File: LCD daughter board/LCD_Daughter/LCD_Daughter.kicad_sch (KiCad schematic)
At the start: 12 parts, among them J1 JST EH 9pos

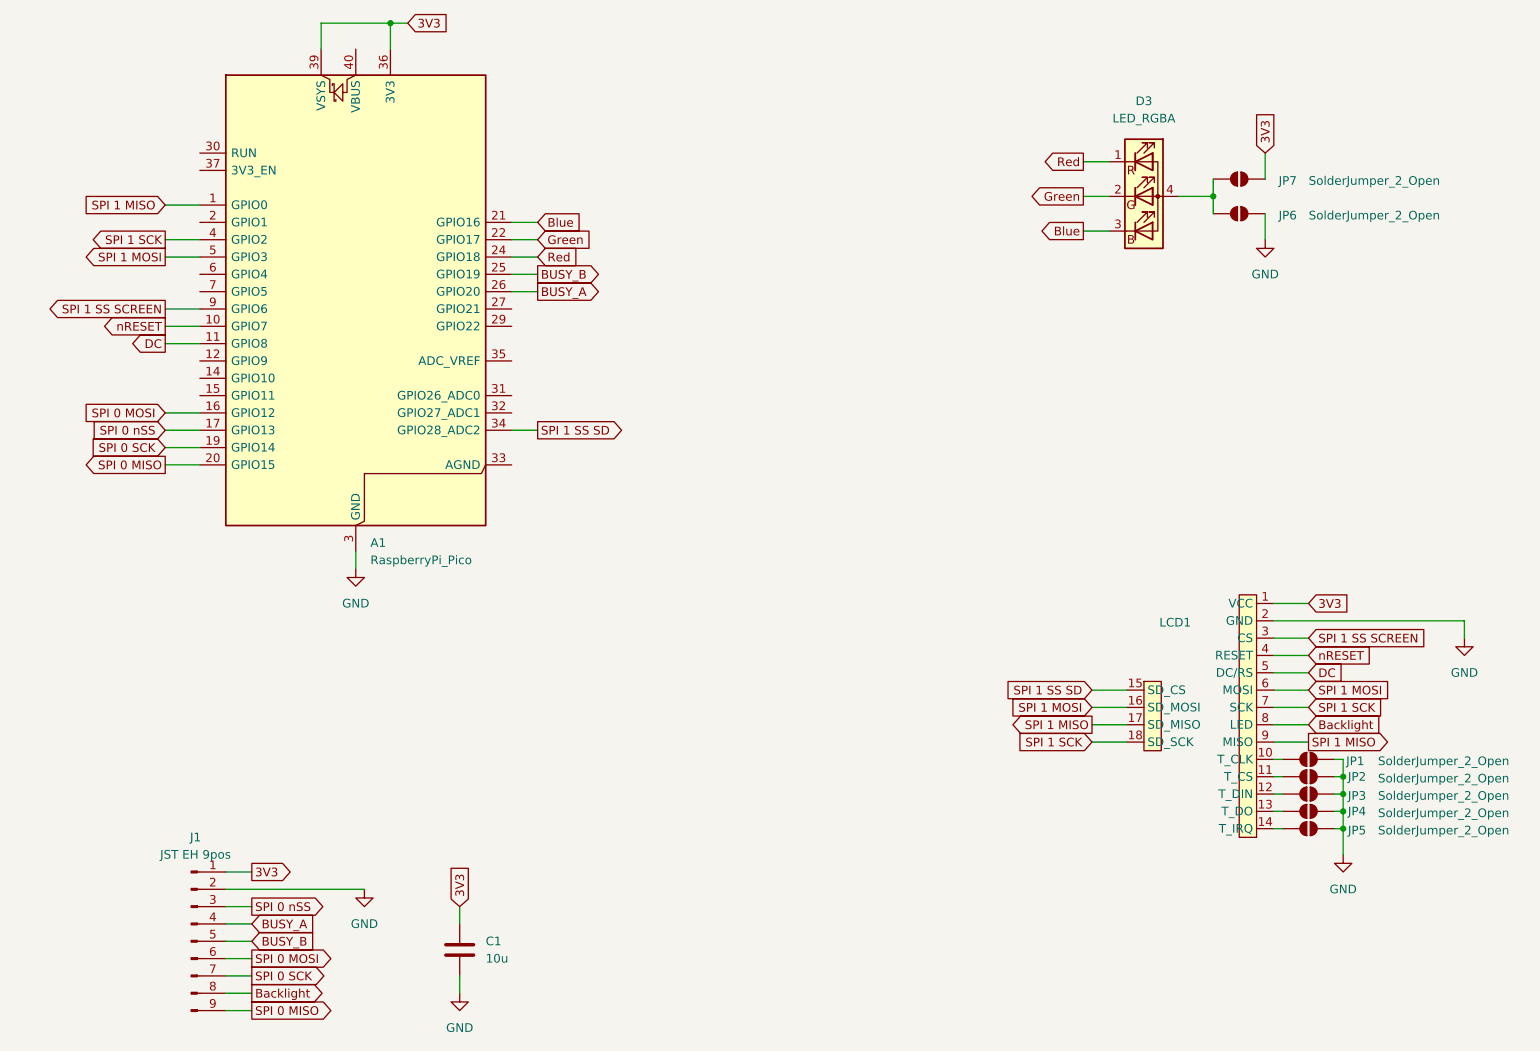
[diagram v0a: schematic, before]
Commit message: Renamed SPI busses to match RPI's names. Fixed code to use the correct SPI busses.
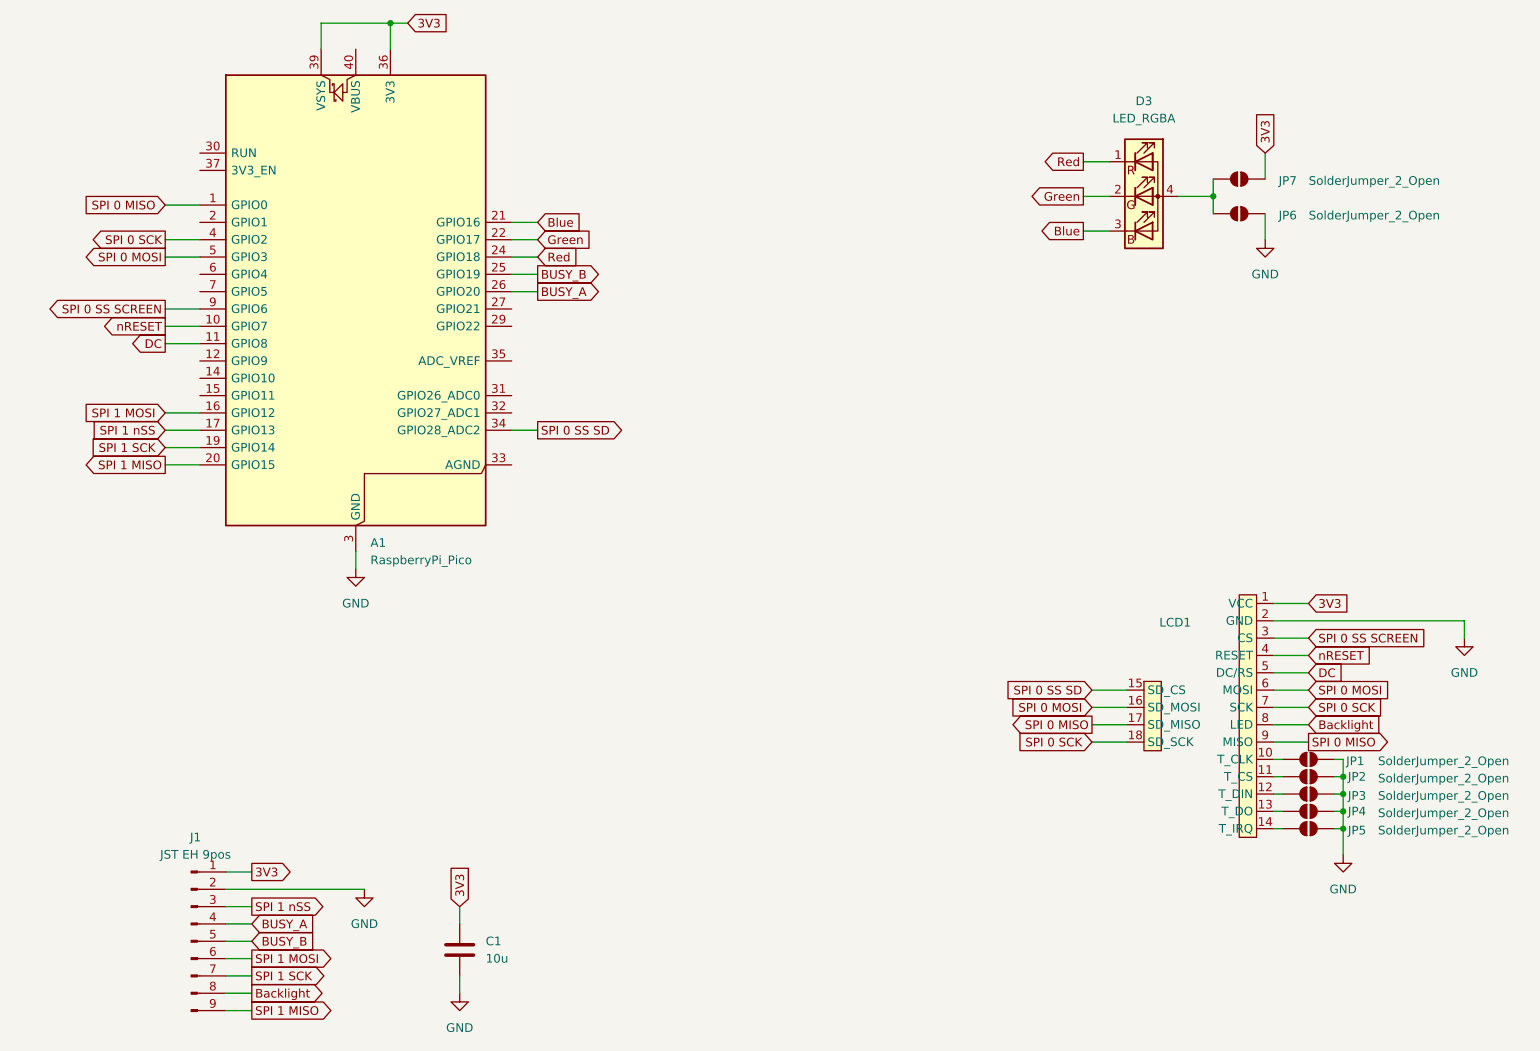
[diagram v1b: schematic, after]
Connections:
- net SPI 0 MISO: now also A1.1 (GPIO0), LCD1.17 (SD_MISO), LCD1.9 (MISO); no longer A1.20 (GPIO15), J1.9 (Pin_9)
- net SPI 0 MOSI: now also A1.5 (GPIO3), LCD1.16 (SD_MOSI), LCD1.6 (MOSI); no longer A1.16 (GPIO12), J1.6 (Pin_6)
- net SPI 0 SCK: now also A1.4 (GPIO2), LCD1.18 (SD_SCK), LCD1.7 (SCK); no longer A1.19 (GPIO14), J1.7 (Pin_7)
- net SPI 1 MISO: now also A1.20 (GPIO15), J1.9 (Pin_9); no longer A1.1 (GPIO0), LCD1.17 (SD_MISO), LCD1.9 (MISO)
- net SPI 1 MOSI: now also A1.16 (GPIO12), J1.6 (Pin_6); no longer A1.5 (GPIO3), LCD1.16 (SD_MOSI), LCD1.6 (MOSI)
- net SPI 1 SCK: now also A1.19 (GPIO14), J1.7 (Pin_7); no longer A1.4 (GPIO2), LCD1.18 (SD_SCK), LCD1.7 (SCK)
- net SPI 0 nSS renamed SPI 1 nSS
- net SPI 1 SS SCREEN renamed SPI 0 SS SCREEN
- net SPI 1 SS SD renamed SPI 0 SS SD
